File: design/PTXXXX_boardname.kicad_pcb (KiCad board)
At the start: 2 copper layers, 0 parts

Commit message: added PCB outline for board size 150mm x 100mm with 1.5mm margin changed board setup and design rules etc... ...changed board type to 4-layer, components both sides, removed Adhesive layers ...set minimum track width/spacing 0.25mm, min via drill/diameter 0.30/0.60mm ...changed all silk/other laters to 0.12mm line thickness, copper to 0.25mm ...changed to require courtyard definitions in footprints ...changed minimum hole to hole to 0.50mm, some web searches say 0.25mm but to be safe ...changed solder mask clearance to 0.065mm, minimum width to 0.10mm as per NCAB DFM best annotated-netlisted and roughly placed M3 Holes in design after last commit changes set origin point, auxiliary axis, and layer alignment target at PCB bottom-left
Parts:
- added H1: M3 Hole, MountingHole:MountingHole_3.5mm_Pad_Via, F.Cu at (86.0, 139.0)
- added H2: M3 Hole, MountingHole:MountingHole_3.5mm_Pad_Via, F.Cu at (86.0, 51.0)
- added H3: M3 Hole, MountingHole:MountingHole_3.5mm_Pad_Via, F.Cu at (224.0, 51.0)
- added H4: M3 Hole, MountingHole:MountingHole_3.5mm_Pad_Via, F.Cu at (224.0, 139.0)
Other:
- board outline added: 150 x 100 mm
- copper layers 2 -> 4
- net class Default: clearance 0.2 -> 0.25; via_dia 0.8 -> 0.6; via_drill 0.4 -> 0.3
- rule pad_to_mask_clearance: 0.051 -> 0.065
- rule solder_mask_min_width: 0.25 -> 0.1
- rule trace_clearance: 0.2 -> 0.25
- rule trace_min: 0.2 -> 0.25
- rule via_min_size: 0.4 -> 0.6
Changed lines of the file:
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@@
   (general
     (thickness 1.6)
-    (drawings 0)
+    (drawings 10)
     (tracks 0)
     (zones 0)
-    (modules 0)
-    (nets 1)
+    (modules 4)
+    (nets 2)
   )
   (page A4)
@@
   (layers
     (0 F.Cu signal)
+    (1 In1.Cu mixed)
+    (2 In2.Cu mixed)
     (31 B.Cu signal)
-    (32 B.Adhes user)
-    (33 F.Adhes user)
     (34 B.Paste user)
     (35 F.Paste user)
@@
   (setup
     (last_trace_width 0.25)
-    (trace_clearance 0.2)
+    (trace_clearance 0.25)
     (zone_clearance 0.508)
     (zone_45_only no)
-    (trace_min 0.2)
-    (via_size 0.8)
-    (via_drill 0.4)
-    (via_min_size 0.4)
+    (trace_min 0.25)
+    (via_size 0.6)
+    (via_drill 0.3)
+    (via_min_size 0.6)
     (via_min_drill 0.3)
     (uvia_size 0.3)
@@
     (uvia_min_drill 0.1)
     (edge_width 0.05)
-    (segment_width 0.2)
-    (pcb_text_width 0.3)
+    (segment_width 0.25)
+    (pcb_text_width 0.25)
     (pcb_text_size 1.5 1.5)
     (mod_edge_width 0.12)
     (mod_text_size 1 1)
-    (mod_text_width 0.15)
+    (mod_text_width 0.12)
     (pad_size 1.524 1.524)
     (pad_drill 0.762)
-    (pad_to_mask_clearance 0.051)
-    (solder_mask_min_width 0.25)
-    (aux_axis_origin 0 0)
+    (pad_to_mask_clearance 0.065)
+    (solder_mask_min_width 0.1)
+    (aux_axis_origin 80 145)
+    (grid_origin 80 145)
     (visible_elements 7FFFFFFF)
     (pcbplotparams
@@
   )
   (net 0 "")
+  (net 1 GND)
   (net_class Default "This is the default net class."
-    (clearance 0.2)
+    (clearance 0.25)
     (trace_width 0.25)
-    (via_dia 0.8)
-    (via_drill 0.4)
+    (via_dia 0.6)
+    (via_drill 0.3)
     (uvia_dia 0.3)
     (uvia_drill 0.1)
-  )
+    (diff_pair_width 0.25)
+    (diff_pair_gap 0.25)
+    (add_net GND)
+  )
+  (module MountingHole:MountingHole_3.5mm_Pad_Via (layer F.Cu)
+    (at 86 139)
+    (descr "Mounting Hole 3.5mm")
+    (tags "mounting hole 3.5mm")
+    (attr virtual)
+    (fp_text reference H1 (at 0 -4.5) (layer F.SilkS)
+      (effects (font (size 1 1) (thickness 0.15)))
+    )
+    (fp_text value "M3 Hole" (at 0 4.5) (layer F.Fab)
+      (effects (font (size 1 1) (thickness 0.15)))
+    )
+    (fp_text user %R (at 0.3 0) (layer F.Fab)
+      (effects (font (size 1 1) (thickness 0.15)))
+    )
+    (fp_circle (center 0 0) (end 3.5 0) (layer Cmts.User) (width 0.15))
+    (fp_circle (center 0 0) (end 3.75 0) (layer F.CrtYd) (width 0.05))
+    (pad 1 thru_hole circle (at 0 0) (size 7 7) (drill 3.5) (layers *.Cu *.Mask)
+      (net 1 GND))
+    (pad 1 thru_hole circle (at 2.625 0) (size 0.8 0.8) (drill 0.5) (layers *.Cu *.Mask)
+      (net 1 GND))
+    (pad 1 thru_hole circle (at 1.856155 1.856155) (size 0.8 0.8) (drill 0.5) (layers *.Cu *.Mask)
+      (net 1 GND))
+    (pad 1 thru_hole circle (at 0 2.625) (size 0.8 0.8) (drill 0.5) (layers *.Cu *.Mask)
+      (net 1 GND))
+    (pad 1 thru_hole circle (at -1.856155 1.856155) (size 0.8 0.8) (drill 0.5) (layers *.Cu *.Mask)
+      (net 1 GND))
+    (pad 1 thru_hole circle (at -2.625 0) (size 0.8 0.8) (drill 0.5) (layers *.Cu *.Mask)
+      (net 1 GND))
+    (pad 1 thru_hole circle (at -1.856155 -1.856155) (size 0.8 0.8) (drill 0.5) (layers *.Cu *.Mask)
+      (net 1 GND))
+    (pad 1 thru_hole circle (at 0 -2.625) (size 0.8 0.8) (drill 0.5) (layers *.Cu *.Mask)
+      (net 1 GND))
+    (pad 1 thru_hole circle (at 1.856155 -1.856155) (size 0.8 0.8) (drill 0.5) (layers *.Cu *.Mask)
+      (net 1 GND))
+  )
+  (module MountingHole:MountingHole_3.5mm_Pad_Via (layer F.Cu)
+    (at 86 51)
+    (descr "Mounting Hole 3.5mm")
+    (tags "mounting hole 3.5mm")
+    (attr virtual)
+    (fp_text reference H2 (at 0 -4.5) (layer F.SilkS)
+      (effects (font (size 1 1) (thickness 0.15)))
+    )
+    (fp_text value "M3 Hole" (at 0 4.5) (layer F.Fab)
+      (effects (font (size 1 1) (thickness 0.15)))
+    )
+    (fp_circle (center 0 0) (end 3.75 0) (layer F.CrtYd) (width 0.05))
+    (fp_circle (center 0 0) (end 3.5 0) (layer Cmts.User) (width 0.15))
+    (fp_text user %R (at 0.3 0) (layer F.Fab)
+      (effects (font (size 1 1) (thickness 0.15)))
+    )
+    (pad 1 thru_hole circle (at 1.856155 -1.856155) (size 0.8 0.8) (drill 0.5) (layers *.Cu *.Mask)
+      (net 1 GND))
+    (pad 1 thru_hole circle (at 0 -2.625) (size 0.8 0.8) (drill 0.5) (layers *.Cu *.Mask)
+      (net 1 GND))
+    (pad 1 thru_hole circle (at -1.856155 -1.856155) (size 0.8 0.8) (drill 0.5) (layers *.Cu *.Mask)
+      (net 1 GND))
+    (pad 1 thru_hole circle (at -2.625 0) (size 0.8 0.8) (drill 0.5) (layers *.Cu *.Mask)
+      (net 1 GND))
+    (pad 1 thru_hole circle (at -1.856155 1.856155) (size 0.8 0.8) (drill 0.5) (layers *.Cu *.Mask)
+      (net 1 GND))
+    (pad 1 thru_hole circle (at 0 2.625) (size 0.8 0.8) (drill 0.5) (layers *.Cu *.Mask)
+      (net 1 GND))
+    (pad 1 thru_hole circle (at 1.856155 1.856155) (size 0.8 0.8) (drill 0.5) (layers *.Cu *.Mask)
+      (net 1 GND))
+    (pad 1 thru_hole circle (at 2.625 0) (size 0.8 0.8) (drill 0.5) (layers *.Cu *.Mask)
+      (net 1 GND))
+    (pad 1 thru_hole circle (at 0 0) (size 7 7) (drill 3.5) (layers *.Cu *.Mask)
+      (net 1 GND))
+  )
+  (module MountingHole:MountingHole_3.5mm_Pad_Via (layer F.Cu)
+    (at 224 51)
+    (descr "Mounting Hole 3.5mm")
+    (tags "mounting hole 3.5mm")
+    (attr virtual)
+    (fp_text reference H3 (at 0 -4.5) (layer F.SilkS)
+      (effects (font (size 1 1) (thickness 0.15)))
+    )
+    (fp_text value "M3 Hole" (at 0 4.5) (layer F.Fab)
+      (effects (font (size 1 1) (thickness 0.15)))
+    )
+    (fp_text user %R (at 0.3 0) (layer F.Fab)
+      (effects (font (size 1 1) (thickness 0.15)))
+    )
+    (fp_circle (center 0 0) (end 3.5 0) (layer Cmts.User) (width 0.15))
+    (fp_circle (center 0 0) (end 3.75 0) (layer F.CrtYd) (width 0.05))
+    (pad 1 thru_hole circle (at 0 0) (size 7 7) (drill 3.5) (layers *.Cu *.Mask)
+      (net 1 GND))
+    (pad 1 thru_hole circle (at 2.625 0) (size 0.8 0.8) (drill 0.5) (layers *.Cu *.Mask)
+      (net 1 GND))
+    (pad 1 thru_hole circle (at 1.856155 1.856155) (size 0.8 0.8) (drill 0.5) (layers *.Cu *.Mask)
+      (net 1 GND))
+    (pad 1 thru_hole circle (at 0 2.625) (size 0.8 0.8) (drill 0.5) (layers *.Cu *.Mask)
+      (net 1 GND))
+    (pad 1 thru_hole circle (at -1.856155 1.856155) (size 0.8 0.8) (drill 0.5) (layers *.Cu *.Mask)
+      (net 1 GND))
+    (pad 1 thru_hole circle (at -2.625 0) (size 0.8 0.8) (drill 0.5) (layers *.Cu *.Mask)
+      (net 1 GND))
+    (pad 1 thru_hole circle (at -1.856155 -1.856155) (size 0.8 0.8) (drill 0.5) (layers *.Cu *.Mask)
+      (net 1 GND))
+    (pad 1 thru_hole circle (at 0 -2.625) (size 0.8 0.8) (drill 0.5) (layers *.Cu *.Mask)
+      (net 1 GND))
+    (pad 1 thru_hole circle (at 1.856155 -1.856155) (size 0.8 0.8) (drill 0.5) (layers *.Cu *.Mask)
+      (net 1 GND))
+  )
+  (module MountingHole:MountingHole_3.5mm_Pad_Via (layer F.Cu)
+    (at 224 139)
+    (descr "Mounting Hole 3.5mm")
+    (tags "mounting hole 3.5mm")
+    (attr virtual)
+    (fp_text reference H4 (at 0 -4.5) (layer F.SilkS)
+      (effects (font (size 1 1) (thickness 0.15)))
+    )
+    (fp_text value "M3 Hole" (at 0 4.5) (layer F.Fab)
+      (effects (font (size 1 1) (thickness 0.15)))
+    )
+    (fp_circle (center 0 0) (end 3.75 0) (layer F.CrtYd) (width 0.05))
+    (fp_circle (center 0 0) (end 3.5 0) (layer Cmts.User) (width 0.15))
+    (fp_text user %R (at 0.3 0) (layer F.Fab)
+      (effects (font (size 1 1) (thickness 0.15)))
+    )
+    (pad 1 thru_hole circle (at 1.856155 -1.856155) (size 0.8 0.8) (drill 0.5) (layers *.Cu *.Mask)
+      (net 1 GND))
+    (pad 1 thru_hole circle (at 0 -2.625) (size 0.8 0.8) (drill 0.5) (layers *.Cu *.Mask)
+      (net 1 GND))
+    (pad 1 thru_hole circle (at -1.856155 -1.856155) (size 0.8 0.8) (drill 0.5) (layers *.Cu *.Mask)
+      (net 1 GND))
+    (pad 1 thru_hole circle (at -2.625 0) (size 0.8 0.8) (drill 0.5) (layers *.Cu *.Mask)
+      (net 1 GND))
+    (pad 1 thru_hole circle (at -1.856155 1.856155) (size 0.8 0.8) (drill 0.5) (layers *.Cu *.Mask)
+      (net 1 GND))
+    (pad 1 thru_hole circle (at 0 2.625) (size 0.8 0.8) (drill 0.5) (layers *.Cu *.Mask)
+      (net 1 GND))
+    (pad 1 thru_hole circle (at 1.856155 1.856155) (size 0.8 0.8) (drill 0.5) (layers *.Cu *.Mask)
+      (net 1 GND))
+    (pad 1 thru_hole circle (at 2.625 0) (size 0.8 0.8) (drill 0.5) (layers *.Cu *.Mask)
+      (net 1 GND))
+    (pad 1 thru_hole circle (at 0 0) (size 7 7) (drill 3.5) (layers *.Cu *.Mask)
+      (net 1 GND))
+  )
+  (target plus (at 80 145) (size 5) (width 0.05) (layer Edge.Cuts))
+  (target plus (at 80 145) (size 5) (width 0.05) (layer Edge.Cuts))
+  (gr_line (start 228.5 143.5) (end 81.5 143.5) (layer Margin) (width 0.15))
+  (gr_line (start 228.5 46.5) (end 228.5 143.5) (layer Margin) (width 0.15))
+  (gr_line (start 81.5 46.5) (end 228.5 46.5) (layer Margin) (width 0.15))
+  (gr_line (start 81.5 143.5) (end 81.5 46.5) (layer Margin) (width 0.15))
+  (gr_line (start 80 45) (end 80 145) (layer Edge.Cuts) (width 0.05))
+  (gr_line (start 230 45) (end 80 45) (layer Edge.Cuts) (width 0.05))
+  (gr_line (start 230 145) (end 230 45) (layer Edge.Cuts) (width 0.05))
+  (gr_line (start 80 145) (end 230 145) (layer Edge.Cuts) (width 0.05))
 )

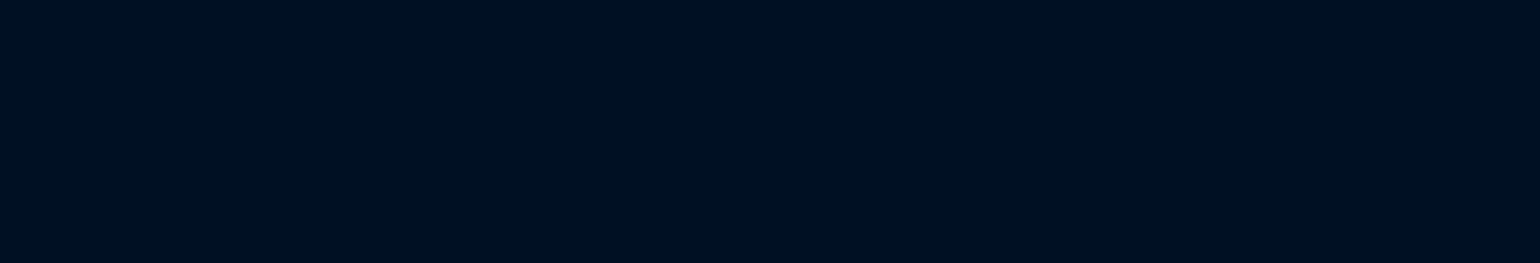
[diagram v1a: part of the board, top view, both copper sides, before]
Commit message: added name & description text for every PCB layer added defined track widths (0.25mm to 3mm) & via sizes (0.3/0.6mm & 0.5/0.9mm)
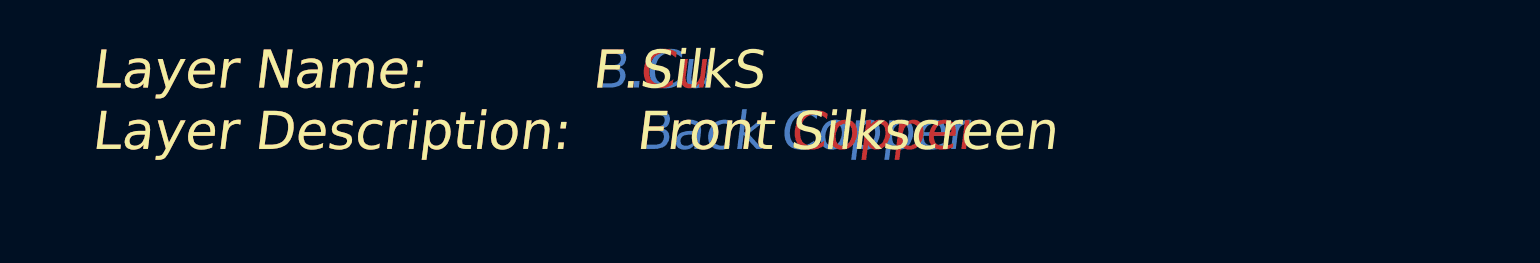
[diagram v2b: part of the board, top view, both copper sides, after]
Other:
- board text added: "Layer Name: B.CrtYd Layer Description: Back Footprint Courtyard"
- board text added: "Layer Name: B.Cu Layer Description: Back Copper"
- board text added: "Layer Name: B.Fab Layer Description: Back Fabrication & Assembly"
- board text added: "Layer Name: B.Mask Layer Description: Back Soldermask"
- board text added: "Layer Name: B.Paste Layer Description: Back Solder Paste"
- board text added: "Layer Name: B.SilkS Layer Description: Back Silkscreen"
- board text added: "Layer Name: Cmts.User Layer Description: User Comments"
- board text added: "Layer Name: Dwgs.User Layer Description: User Drawings"
- board text added: "Layer Name: Eco1.User Layer Description: Other Documentation Layer"
- board text added: "Layer Name: Eco2.User Layer Description: Other Documentation Layer"
- board text added: "Layer Name: F.CrtYd Layer Description: Front Footprint Courtyard"
- board text added: "Layer Name: F.Cu Layer Description: Front Copper"
- board text added: "Layer Name: F.Fab Layer Description: Front Fabrication & Assembly"
- board text added: "Layer Name: F.Mask Layer Description: Front Soldermask"
- board text added: "Layer Name: F.Paste Layer Description: Front Solder Paste"
- board text added: "Layer Name: F.SilkS Layer Description: Front Silkscreen"
- board text added: "Layer Name: In1.Cu Layer Description: Inner Layer-1 Copper"
- board text added: "Layer Name: In2.Cu Layer Description: Inner Layer-2 Copper"
- board text added: "Layer Name: Margin Layer Description: Board Edge Placement Margin"
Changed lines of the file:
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@@
   (general
     (thickness 1.6)
-    (drawings 10)
+    (drawings 29)
     (tracks 0)
     (zones 0)
@@
   (setup
     (last_trace_width 0.25)
+    (user_trace_width 0.25)
+    (user_trace_width 0.35)
+    (user_trace_width 0.5)
+    (user_trace_width 0.7)
+    (user_trace_width 1)
+    (user_trace_width 1.4)
+    (user_trace_width 2)
+    (user_trace_width 3)
     (trace_clearance 0.25)
     (zone_clearance 0.508)
@@
     (via_min_size 0.6)
     (via_min_drill 0.3)
+    (user_via 0.6 0.3)
+    (user_via 0.9 0.5)
     (uvia_size 0.3)
     (uvia_drill 0.1)
@@
       (net 1 GND))
   )
+  (gr_text "Layer Name:          In2.Cu\nLayer Description:    Inner Layer-2 Copper" (at 106 23) (layer In2.Cu)
+    (effects (font (size 2.5 2.5) (thickness 0.25) italic) (justify left))
+  )
+  (gr_text "Layer Name:          In1.Cu\nLayer Description:    Inner Layer-1 Copper" (at 106 23) (layer In1.Cu)
+    (effects (font (size 2.5 2.5) (thickness 0.25) italic) (justify left))
+  )
+  (gr_text "Layer Name:          Eco1.User\nLayer Description:    Other Documentation Layer" (at 106 23) (layer Eco1.User)
+    (effects (font (size 2.5 2.5) (thickness 0.25) italic) (justify left))
+  )
+  (gr_text "Layer Name:          Eco2.User\nLayer Description:    Other Documentation Layer" (at 106 23) (layer Eco2.User)
+    (effects (font (size 2.5 2.5) (thickness 0.25) italic) (justify left))
+  )
+  (gr_text "Layer Name:          Margin\nLayer Description:    Board Edge Placement Margin" (at 106 23) (layer Margin)
+    (effects (font (size 2.5 2.5) (thickness 0.25) italic) (justify left))
+  )
+  (gr_text "Layer Name:          B.CrtYd\nLayer Description:    Back Footprint Courtyard" (at 106 23) (layer B.CrtYd)
+    (effects (font (size 2.5 2.5) (thickness 0.25) italic) (justify left))
+  )
+  (gr_text "Layer Name:          F.CrtYd\nLayer Description:    Front Footprint Courtyard" (at 106 23) (layer F.CrtYd)
+    (effects (font (size 2.5 2.5) (thickness 0.25) italic) (justify left))
+  )
+  (gr_text "Layer Name:          F.Mask\nLayer Description:    Front Soldermask" (at 105.8 23.05) (layer F.Mask)
+    (effects (font (size 2.5 2.5) (thickness 0.25) italic) (justify left))
+  )
+  (gr_text "Layer Name:          Cmts.User\nLayer Description:    User Comments" (at 105.8 23.05) (layer Cmts.User)
+    (effects (font (size 2.5 2.5) (thickness 0.25) italic) (justify left))
+  )
+  (gr_text "Layer Name:          F.SilkS\nLayer Description:    Front Silkscreen" (at 105.8 23.05) (layer F.SilkS)
+    (effects (font (size 2.5 2.5) (thickness 0.25) italic) (justify left))
+  )
+  (gr_text "Layer Name:          F.Fab\nLayer Description:    Front Fabrication & Assembly" (at 105.8 23.05) (layer F.Fab)
+    (effects (font (size 2.5 2.5) (thickness 0.25) italic) (justify left))
+  )
+  (gr_text "Layer Name:          B.Mask\nLayer Description:    Back Soldermask" (at 105.8 23.05) (layer B.Mask)
+    (effects (font (size 2.5 2.5) (thickness 0.25) italic) (justify left))
+  )
+  (gr_text "Layer Name:          Dwgs.User\nLayer Description:    User Drawings" (at 105.8 23.05) (layer Dwgs.User)
+    (effects (font (size 2.5 2.5) (thickness 0.25) italic) (justify left))
+  )
+  (gr_text "Layer Name:          B.Fab\nLayer Description:    Back Fabrication & Assembly" (at 105.8 23.05) (layer B.Fab)
+    (effects (font (size 2.5 2.5) (thickness 0.25) italic) (justify left))
+  )
+  (gr_text "Layer Name:          B.Paste\nLayer Description:    Back Solder Paste" (at 105.8 23.05) (layer B.Paste)
+    (effects (font (size 2.5 2.5) (thickness 0.25) italic) (justify left))
+  )
+  (gr_text "Layer Name:          B.Cu\nLayer Description:    Back Copper" (at 105.8 23.05) (layer B.Cu)
+    (effects (font (size 2.5 2.5) (thickness 0.25) italic) (justify left))
+  )
+  (gr_text "Layer Name:          B.SilkS\nLayer Description:    Back Silkscreen" (at 105.8 23.05) (layer B.SilkS)
+    (effects (font (size 2.5 2.5) (thickness 0.25) italic) (justify left))
+  )
+  (gr_text "Layer Name:          F.Cu\nLayer Description:    Front Copper" (at 105.8 23.05) (layer F.Cu)
+    (effects (font (size 2.5 2.5) (thickness 0.25) italic) (justify left))
+  )
+  (gr_text "Layer Name:          F.Paste\nLayer Description:    Front Solder Paste" (at 105.8 23.05) (layer F.Paste)
+    (effects (font (size 2.5 2.5) (thickness 0.25) italic) (justify left))
+  )
   (target plus (at 80 145) (size 5) (width 0.05) (layer Edge.Cuts))
